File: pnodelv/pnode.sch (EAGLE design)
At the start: 41 parts, among them IC2 HTU21D, IC3 SI4012

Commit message: Routing for pnodelv
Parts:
- added U$4: 4.7u, jonsowman:BOURNS_SDE0403A
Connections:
- new net N$6: U$2.SW, U$4.P$2
- net GND: now also JP1.1
- net VBATT: now also U$4.P$1
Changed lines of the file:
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@@
 <part name="C3" library="passives-7351" deviceset="CAPACITOR" device="0603-N" value="4.7u"/>
 <part name="C10" library="passives-7351" deviceset="CAPACITOR" device="0603-N" value="10u"/>
+<part name="U$4" library="jonsowman" deviceset="BOURNS_SDE0403A" device="" value="4.7u"/>
 </parts>
 <sheets>
@@
 <instance part="C3" gate="G$1" x="5.08" y="104.14"/>
 <instance part="C10" gate="G$1" x="43.18" y="111.76"/>
+<instance part="U$4" gate="G$1" x="10.16" y="124.46"/>
 </instances>
 <busses>
@@
 <pinref part="GND1" gate="1" pin="GND"/>
 <wire x1="-12.7" y1="111.76" x2="-12.7" y2="109.22" width="0.1524" layer="91"/>
+<pinref part="JP1" gate="G$1" pin="1"/>
 </segment>
 <segment>
@@
 <wire x1="5.08" y1="109.22" x2="5.08" y2="106.68" width="0.1524" layer="91"/>
 <junction x="5.08" y="109.22"/>
+<pinref part="U$4" gate="G$1" pin="P$1"/>
+<wire x1="2.54" y1="124.46" x2="2.54" y2="116.84" width="0.1524" layer="91"/>
+<wire x1="2.54" y1="116.84" x2="5.08" y2="116.84" width="0.1524" layer="91"/>
+<wire x1="5.08" y1="116.84" x2="5.08" y2="114.3" width="0.1524" layer="91"/>
 </segment>
 </net>
@@
 </segment>
 </net>
+<net name="N$6" class="0">
+<segment>
+<pinref part="U$4" gate="G$1" pin="P$2"/>
+<pinref part="U$2" gate="G$1" pin="SW"/>
+<wire x1="17.78" y1="124.46" x2="20.32" y2="124.46" width="0.1524" layer="91"/>
+</segment>
+</net>

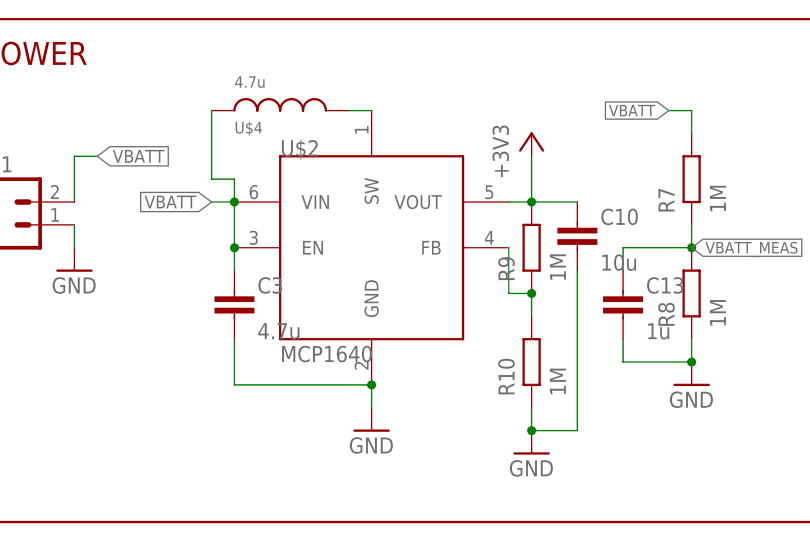
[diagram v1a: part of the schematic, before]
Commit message: Added silk and submitted gerbers for pnodelv
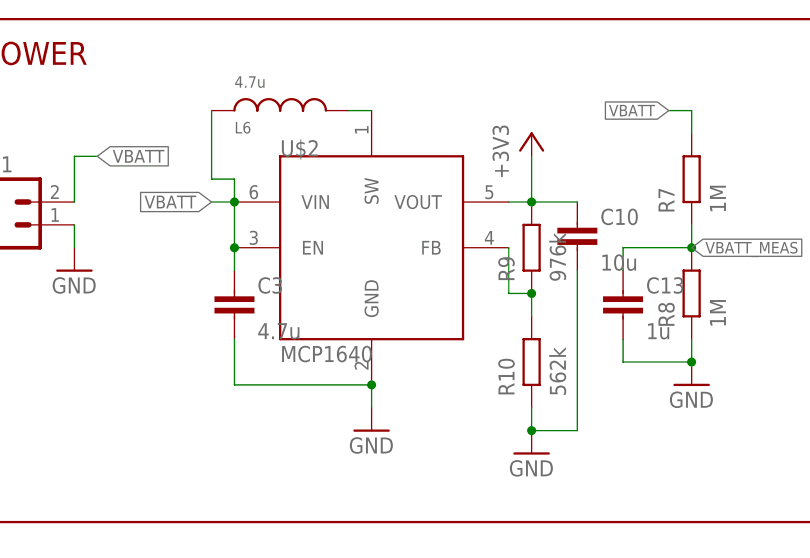
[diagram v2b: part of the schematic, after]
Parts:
- R10: value 1M -> 562k
- R9: value 1M -> 976k
- renumbered U$4 to L6
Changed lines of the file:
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@@
 <part name="GND8" library="supply1" deviceset="GND" device=""/>
 <part name="JP1" library="Mine" deviceset="M02" device="PTH"/>
-<part name="R9" library="passives-7351" deviceset="RESISTOR" device="0603-N" value="1M"/>
-<part name="R10" library="passives-7351" deviceset="RESISTOR" device="0603-N" value="1M"/>
+<part name="R9" library="passives-7351" deviceset="RESISTOR" device="0603-N" value="976k"/>
+<part name="R10" library="passives-7351" deviceset="RESISTOR" device="0603-N" value="562k"/>
 <part name="GND20" library="supply1" deviceset="GND" device=""/>
 <part name="C3" library="passives-7351" deviceset="CAPACITOR" device="0603-N" value="4.7u"/>
 <part name="C10" library="passives-7351" deviceset="CAPACITOR" device="0603-N" value="10u"/>
-<part name="U$4" library="jonsowman" deviceset="BOURNS_SDE0403A" device="" value="4.7u"/>
+<part name="L6" library="jonsowman" deviceset="BOURNS_SDE0403A" device="" value="4.7u"/>
 </parts>
 <sheets>
@@
 <instance part="C3" gate="G$1" x="5.08" y="104.14"/>
 <instance part="C10" gate="G$1" x="43.18" y="111.76"/>
-<instance part="U$4" gate="G$1" x="10.16" y="124.46"/>
+<instance part="L6" gate="G$1" x="10.16" y="124.46"/>
 </instances>
 <busses>
@@
 <wire x1="5.08" y1="109.22" x2="5.08" y2="106.68" width="0.1524" layer="91"/>
 <junction x="5.08" y="109.22"/>
-<pinref part="U$4" gate="G$1" pin="P$1"/>
+<pinref part="L6" gate="G$1" pin="P$1"/>
 <wire x1="2.54" y1="124.46" x2="2.54" y2="116.84" width="0.1524" layer="91"/>
 <wire x1="2.54" y1="116.84" x2="5.08" y2="116.84" width="0.1524" layer="91"/>
@@
 <net name="N$6" class="0">
 <segment>
-<pinref part="U$4" gate="G$1" pin="P$2"/>
+<pinref part="L6" gate="G$1" pin="P$2"/>
 <pinref part="U$2" gate="G$1" pin="SW"/>
 <wire x1="17.78" y1="124.46" x2="20.32" y2="124.46" width="0.1524" layer="91"/>

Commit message: switched to smd swd header
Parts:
- removed U$3: SWD_PTH_SHROUD, jonsowman:SWD_PTH_SHROUD
- added J1: SWD_SHROUD_SMD, dtb:SWD_SHROUD_SMD
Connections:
- net +3V3: now also J1.VCC; no longer U$3.VCC
- net GND: now also J1.GND1, J1.GND2, J1.GNDD, J1.KEY; no longer U$3.GND1, U$3.GND2, U$3.GNDD, U$3.KEY
- net NRST: now also J1.NRST; no longer U$3.NRST
- net SWCLK: now also J1.SWCLK; no longer U$3.SWCLK
- net SWDAT: now also J1.SWDAT; no longer U$3.SWDAT
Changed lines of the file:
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@@
 <part name="+3V6" library="supply1" deviceset="+3V3" device=""/>
 <part name="STM32" library="dtb" deviceset="STM32F030F4" device=""/>
-<part name="U$3" library="jonsowman" deviceset="SWD_PTH_SHROUD" device=""/>
 <part name="+3V3" library="supply1" deviceset="+3V3" device=""/>
 <part name="GND3" library="supply1" deviceset="GND" device=""/>
@@
 <part name="C10" library="passives-7351" deviceset="CAPACITOR" device="0603-N" value="10u"/>
 <part name="L6" library="jonsowman" deviceset="BOURNS_SDE0403A" device="" value="4.7u"/>
+<part name="J1" library="dtb" deviceset="SWD_SHROUD" device="_SMD"/>
 </parts>
 <sheets>
@@
 <instance part="+3V6" gate="G$1" x="203.2" y="129.54"/>
 <instance part="STM32" gate="G$1" x="10.16" y="43.18"/>
-<instance part="U$3" gate="G$1" x="27.94" y="-15.24"/>
 <instance part="+3V3" gate="G$1" x="10.16" y="-5.08"/>
 <instance part="GND3" gate="1" x="10.16" y="-25.4"/>
@@
 <instance part="C10" gate="G$1" x="43.18" y="111.76"/>
 <instance part="L6" gate="G$1" x="10.16" y="124.46"/>
+<instance part="J1" gate="G$1" x="27.94" y="-15.24"/>
 </instances>
 <busses>
@@
 </segment>
 <segment>
-<pinref part="U$3" gate="G$1" pin="GND1"/>
 <wire x1="12.7" y1="-12.7" x2="10.16" y2="-12.7" width="0.1524" layer="91"/>
-<pinref part="U$3" gate="G$1" pin="GND2"/>
 <wire x1="12.7" y1="-15.24" x2="10.16" y2="-15.24" width="0.1524" layer="91"/>
 <wire x1="10.16" y1="-12.7" x2="10.16" y2="-15.24" width="0.1524" layer="91"/>
-<pinref part="U$3" gate="G$1" pin="KEY"/>
 <wire x1="12.7" y1="-17.78" x2="10.16" y2="-17.78" width="0.1524" layer="91"/>
 <wire x1="10.16" y1="-15.24" x2="10.16" y2="-17.78" width="0.1524" layer="91"/>
@@
 <wire x1="10.16" y1="-17.78" x2="10.16" y2="-20.32" width="0.1524" layer="91"/>
 <junction x="10.16" y="-17.78"/>
-<pinref part="U$3" gate="G$1" pin="GNDD"/>
 <wire x1="10.16" y1="-20.32" x2="12.7" y2="-20.32" width="0.1524" layer="91"/>
 <pinref part="GND3" gate="1" pin="GND"/>
 <wire x1="10.16" y1="-20.32" x2="10.16" y2="-22.86" width="0.1524" layer="91"/>
 <junction x="10.16" y="-20.32"/>
+<pinref part="J1" gate="G$1" pin="GNDD"/>
+<pinref part="J1" gate="G$1" pin="KEY"/>
+<pinref part="J1" gate="G$1" pin="GND2"/>
+<pinref part="J1" gate="G$1" pin="GND1"/>
 </segment>
 <segment>
@@
 <pinref part="+3V3" gate="G$1" pin="+3V3"/>
 <wire x1="10.16" y1="-7.62" x2="10.16" y2="-10.16" width="0.1524" layer="91"/>
-<pinref part="U$3" gate="G$1" pin="VCC"/>
 <wire x1="10.16" y1="-10.16" x2="12.7" y2="-10.16" width="0.1524" layer="91"/>
+<pinref part="J1" gate="G$1" pin="VCC"/>
 </segment>
 <segment>
@@
 <net name="SWDAT" class="0">
 <segment>
-<pinref part="U$3" gate="G$1" pin="SWDAT"/>
 <wire x1="43.18" y1="-10.16" x2="45.72" y2="-10.16" width="0.1524" layer="91"/>
 <label x="45.72" y="-10.16" size="1.27" layer="95" font="vector" xref="yes"/>
+<pinref part="J1" gate="G$1" pin="SWDAT"/>
 </segment>
 <segment>
@@
 <net name="SWCLK" class="0">
 <segment>
-<pinref part="U$3" gate="G$1" pin="SWCLK"/>
 <wire x1="43.18" y1="-12.7" x2="45.72" y2="-12.7" width="0.1524" layer="91"/>
 <label x="45.72" y="-12.7" size="1.27" layer="95" font="vector" xref="yes"/>
+<pinref part="J1" gate="G$1" pin="SWCLK"/>
 </segment>
 <segment>
@@
 <net name="NRST" class="0">
 <segment>
-<pinref part="U$3" gate="G$1" pin="NRST"/>
 <wire x1="43.18" y1="-20.32" x2="45.72" y2="-20.32" width="0.1524" layer="91"/>
 <label x="45.72" y="-20.32" size="1.27" layer="95" font="vector" xref="yes"/>
-</segment>
-<segment>
+<pinref part="J1" gate="G$1" pin="NRST"/>
+</segment>
+<segment>
